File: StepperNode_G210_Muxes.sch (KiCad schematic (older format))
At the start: 6 parts

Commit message: Add DAC Pages
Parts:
- removed C? (x3): 104, symbol C_Small
- removed U? (x3): 74HCT157, symbol 74HCT157
- added P? (x3): CONN_01X08_2MNT, symbol CONN_01X08_2MNT
- added U? (x3): 74HCT157, symbol 74HCT157
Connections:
- net labels added: STEP_DIR_CTRL
- wire segments 54 -> 60
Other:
- note added: "15TTL load output capacity"
- note added: "At 5V, VinH = 2V\nSafe to interface with 3.3V"
- note added: "Fwd Left and Aft Left Gimbal Controller"
- note added: "Fwd Right and Aft Right Gimbal Controller"
- note added: "Left and Right brake controller."
- note added: "Original Author: SafetyLok"
- note added: "Step 1 and 2, Left and Right brake drive controllers."
- note added: "Step 3 and 4, Fwd Left and Aft Left Gimbal"
- note added: "Step 5 and 6, Fwd Right and Aft Right Gimbal"
- note added: "The purpose of this block is to route 6 Step and 6 Direction signals from each of the two teensys and also buffer those signals.\n"
- note added: "Twisted pair wiring\nGrounded at this end only"
- note removed: "StepperNode_G210_Muxes"

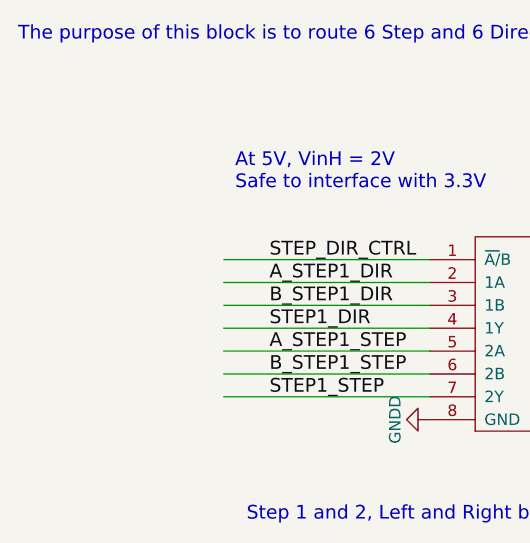
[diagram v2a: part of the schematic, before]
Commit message: Setup DAC channel B
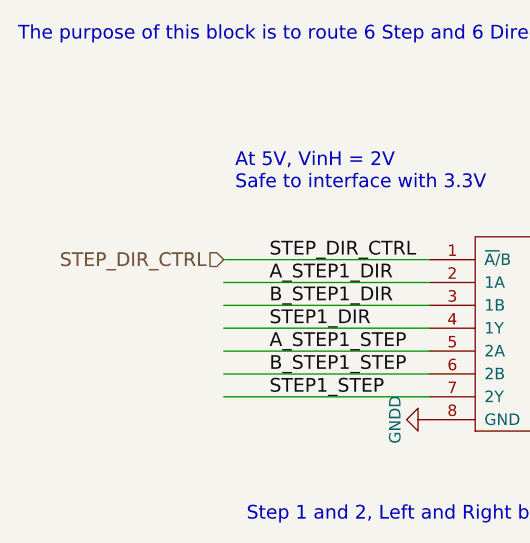
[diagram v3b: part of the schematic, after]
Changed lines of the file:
@@
 $Descr A3 16535 11693
 encoding utf-8
-Sheet 4 8
+Sheet 4 9
 Title "G210 Multiplexers"
 Date ""
@@
 	1    0    0    -1
 $EndComp
+Text HLabel 1500 1600 0    60   Input ~ 0
+STEP_DIR_CTRL
 $EndSCHEMATC

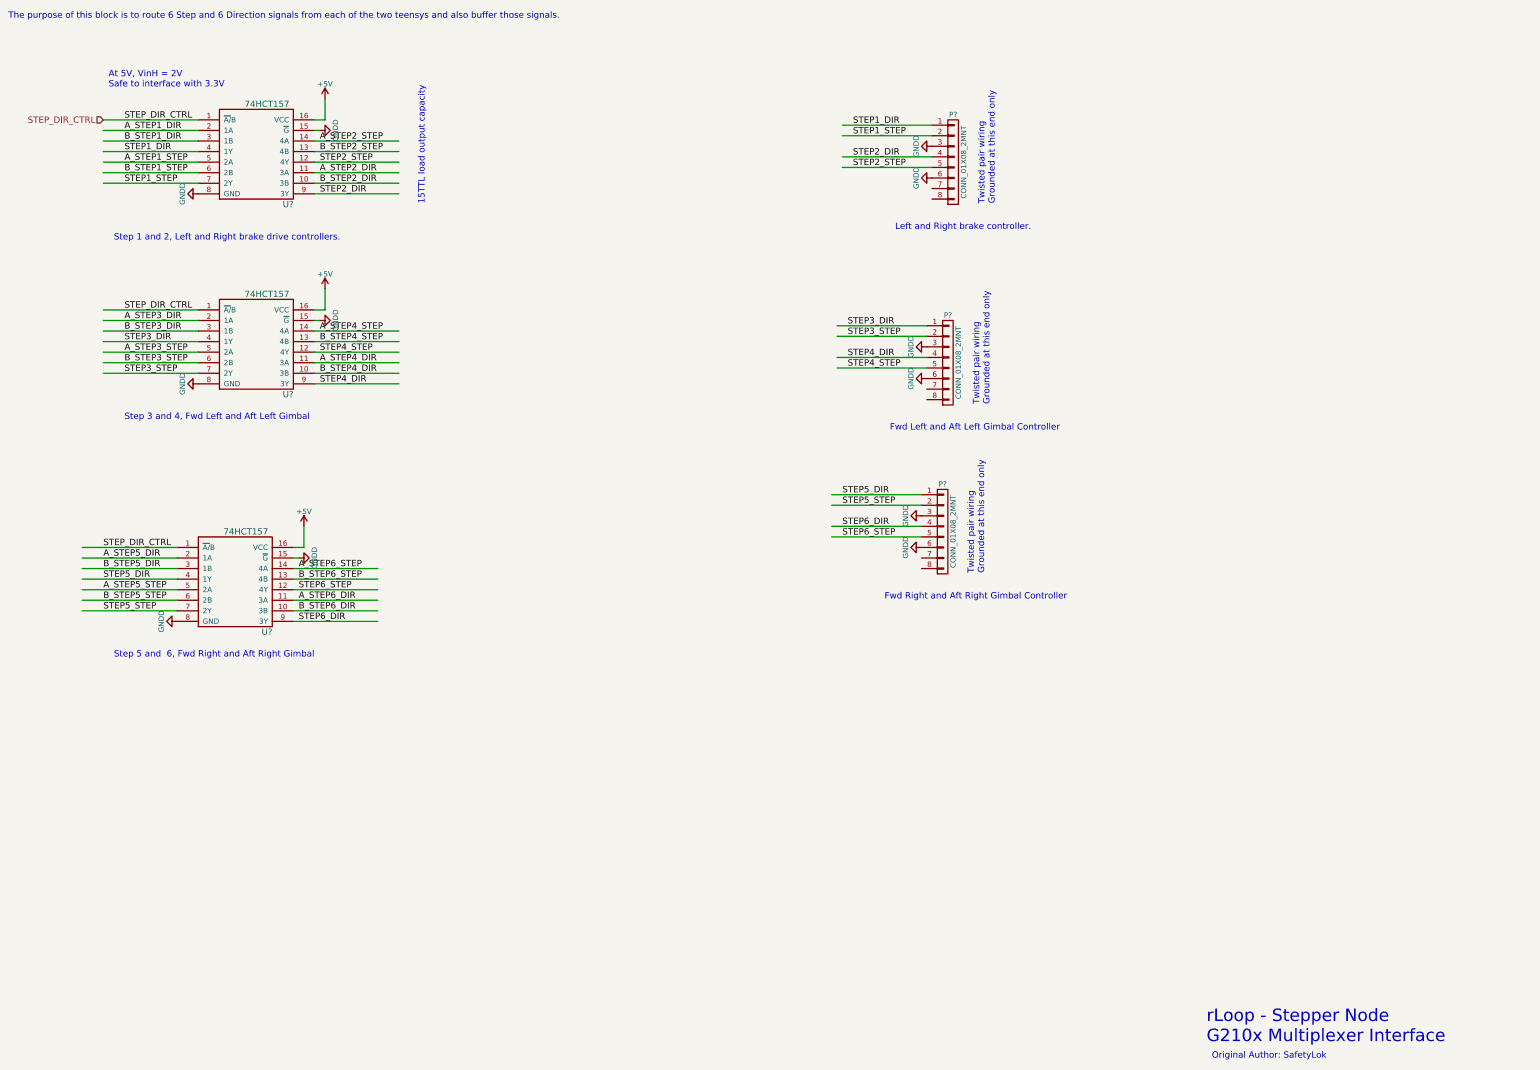
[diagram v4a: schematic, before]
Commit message: Added Sheets for Gimbal, Pusher Interlock and Accels
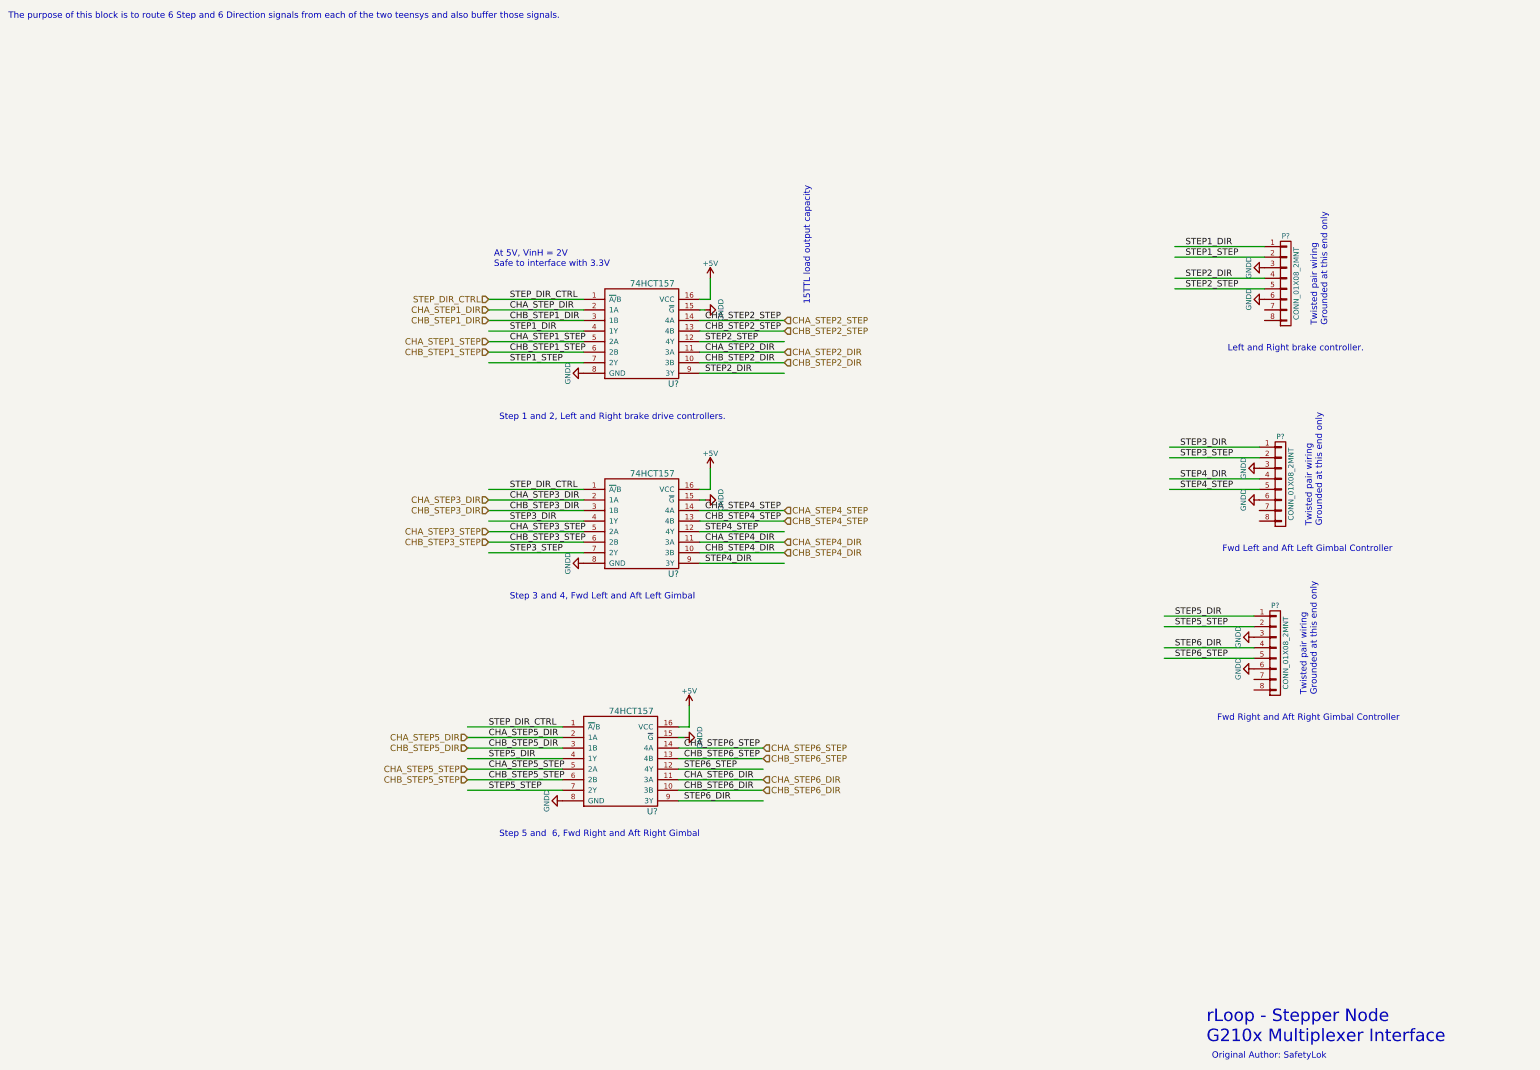
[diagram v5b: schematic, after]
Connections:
- net labels added: CHA_STEP1_DIR, CHA_STEP1_STEP, CHA_STEP2_DIR, CHA_STEP2_STEP, CHA_STEP3_DIR, CHA_STEP3_STEP, CHA_STEP4_DIR, CHA_STEP4_STEP, CHA_STEP5_DIR, CHA_STEP5_STEP, CHA_STEP6_DIR, CHA_STEP6_STEP, CHA_STEP_DIR, CHB_STEP1_DIR, CHB_STEP1_STEP, CHB_STEP2_DIR, CHB_STEP2_STEP, CHB_STEP3_DIR, CHB_STEP3_STEP, CHB_STEP4_DIR, CHB_STEP4_STEP, CHB_STEP5_DIR, CHB_STEP5_STEP, CHB_STEP6_DIR, CHB_STEP6_STEP
- net labels removed: A_STEP1_DIR, A_STEP1_STEP, A_STEP2_DIR, A_STEP2_STEP, A_STEP3_DIR, A_STEP3_STEP, A_STEP4_DIR, A_STEP4_STEP, A_STEP5_DIR, A_STEP5_STEP, A_STEP6_DIR, A_STEP6_STEP, B_STEP1_DIR, B_STEP1_STEP, B_STEP2_DIR, B_STEP2_STEP, B_STEP3_DIR, B_STEP3_STEP, B_STEP4_DIR, B_STEP4_STEP, B_STEP5_DIR, B_STEP5_STEP, B_STEP6_DIR, B_STEP6_STEP
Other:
- moved on the sheet: P?, U?
